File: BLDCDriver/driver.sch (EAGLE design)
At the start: 60 parts, among them Q2 SIZ240DT-T1-GE3, Q3 SIZ240DT-T1-GE3, Q4 SIZ240DT-T1-GE3, U1 QFN50P400X400X100-25NDRV8300D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, U2 AS5048A-HTSP-500, U4 SOP80P620X125-8N, X2 JST-XH-06-PIN-LONG-PAD

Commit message: 配線頑張った
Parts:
- removed D7, D8: WHITE, SparkFun-LED:LED-WHITE0603
- removed R21, R22: 1k, Custom_Designed_By_Yusei:RESISTOR-0603-1/10W-1%
- added C10, C18: 0.1UF, Custom_Designed_By_Yusei:0.1UF_1608
- added REG: AP7333, SOT95P237X112-3N:AP7333
- added U3: MCP2562-E/SN, MCP2562-E_SN:MCP2562-E/SN
- C13: value 0.1UF_1608 -> 0.1UF
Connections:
- net POWERLED_RESISTOR renamed L
- removed net LED1: D7.A
- removed net LED2: D8.A
- removed net N$12: D8.C, R21.1
- removed net N$13: D7.C, R22.1
- new net CANRX: U3.RXD
- new net CANTX: U3.TXD
- net 3V3: now also C10.1, REG.OUT, U3.VIO
- net 5V: now also C18.1, REG.IN, U3.VDD
- net CANH: now also U3.CANH
- net CANL: now also U3.CANL
- net GND: now also C10.2, C18.2, REG.GND, U3.STBY, U3.VSS; no longer R21.2, R22.2

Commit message: FETにビア通した
# ==== Emojis ====
# ✨ :sparkles: Add new feature
# ✅  :white_check_mark: Update existing feature (not bug)
# ⚠️  :warning: Fix bug/error
# 🔥  :fire: Remove files or features
# ✏️ :pencil2: Fix typos
# 📝  :memo: Update documentation
# ♻️  :recycle: Dependencies update
# 🐧  :penguin: Improved the Linux
# 🍎  :apple: Improved the macOS
# 🔖 :bookmark: Add new library
# 🎉  :tada: Initial commit

# ==== Format ====
# :emoji: Subject
#
# Commit body...

# ==== Messages ====
# 新規(ファイル)機能追加: Add
# 機能修正、既存機能追加（バグではない): Update
# リファクタリング: Clean
# ファイル名変更:
# 削除など: Remove
# バグ修正: Fix
# バージョンアップ: Upgrade
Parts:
- removed C13: 0.1UF, Custom_Designed_By_Yusei:0.1UF_1608
- added R21: 10k, Custom_Designed_By_Yusei:RESISTOR-0603-1/10W-1%
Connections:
- net 3V3: now also R21.1
- net GND: no longer C13.2
- net NRST: now also R21.2; no longer C13.1
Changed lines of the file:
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@@
 <setting verticaltext="up"/>
 </settings>
-<grid distance="0.05" unitdist="inch" unit="inch" style="lines" multiple="1" display="no" altdistance="0.01" altunitdist="inch" altunit="inch"/>
+<grid distance="0.1" unitdist="inch" unit="inch" style="lines" multiple="1" display="no" altdistance="0.01" altunitdist="inch" altunit="inch"/>
 <layers>
 <layer number="1" name="Top" color="4" fill="1" visible="no" active="no"/>
@@
 <part name="C11" library="SparkFun-Capacitors" deviceset="0.1UF" device="-0603-100V-10%" value="0.1uF"/>
 <part name="C12" library="SparkFun-Capacitors" deviceset="0.1UF" device="-0603-100V-10%" value="0.1uF"/>
-<part name="C13" library="Custom_Designed_By_Yusei" library_urn="urn:adsk.eagle:library:17377793" deviceset="0.1UF_1608" device="" package3d_urn="urn:adsk.eagle:package:17412407/2" value="0.1UF"/>
 <part name="GND17" library="supply" deviceset="GND" device=""/>
 <part name="R18" library="Custom_Designed_By_Yusei" library_urn="urn:adsk.eagle:library:17377793" deviceset="RESISTOR" device="-0603-1/10W-1%" package3d_urn="urn:adsk.eagle:package:17422883/2" value="10k"/>
@@
 <part name="C18" library="Custom_Designed_By_Yusei" library_urn="urn:adsk.eagle:library:17377793" deviceset="0.1UF_1608" device="" package3d_urn="urn:adsk.eagle:package:17412407/2" value="0.1UF"/>
 <part name="C10" library="Custom_Designed_By_Yusei" library_urn="urn:adsk.eagle:library:17377793" deviceset="0.1UF_1608" device="" package3d_urn="urn:adsk.eagle:package:17412407/2" value="0.1UF"/>
+<part name="R21" library="Custom_Designed_By_Yusei" library_urn="urn:adsk.eagle:library:17377793" deviceset="RESISTOR" device="-0603-1/10W-1%" package3d_urn="urn:adsk.eagle:package:17422883/2" value="10k"/>
 </parts>
 <sheets>
@@
 <attribute name="VALUE" x="169.164" y="197.231" size="1.778" layer="96" font="vector" rot="R270"/>
 </instance>
-<instance part="C13" gate="C$1" x="152.4" y="133.985" smashed="yes">
-<attribute name="NAME" x="153.924" y="136.906" size="1.778" layer="95" font="vector"/>
-</instance>
-<instance part="GND17" gate="1" x="152.4" y="126.365" smashed="yes">
-<attribute name="VALUE" x="149.86" y="123.825" size="1.778" layer="96"/>
+<instance part="GND17" gate="1" x="132.08" y="126.365" smashed="yes">
+<attribute name="VALUE" x="129.54" y="123.825" size="1.778" layer="96"/>
 </instance>
 <instance part="R18" gate="G$1" x="132.08" y="137.795" smashed="yes" rot="R90">
@@
 <instance part="C10" gate="C$1" x="229.87" y="57.15" smashed="yes">
 <attribute name="NAME" x="231.394" y="54.991" size="1.778" layer="95" font="vector"/>
+</instance>
+<instance part="R21" gate="G$1" x="157.48" y="137.16" smashed="yes" rot="R90">
+<attribute name="NAME" x="155.956" y="137.16" size="1.778" layer="95" font="vector" rot="R90" align="bottom-center"/>
+<attribute name="VALUE" x="159.004" y="137.16" size="1.778" layer="96" font="vector" rot="R90" align="top-center"/>
 </instance>
 </instances>
@@
 </segment>
 <segment>
-<pinref part="C13" gate="C$1" pin="2"/>
 <pinref part="GND17" gate="1" pin="GND"/>
-<wire x1="152.4" y1="131.445" x2="152.4" y2="128.905" width="0.1524" layer="91"/>
 <pinref part="R18" gate="G$1" pin="1"/>
 <wire x1="132.08" y1="132.715" x2="132.08" y2="128.905" width="0.1524" layer="91"/>
-<wire x1="132.08" y1="128.905" x2="152.4" y2="128.905" width="0.1524" layer="91"/>
-<junction x="152.4" y="128.905"/>
 <wire x1="119.38" y1="132.715" x2="119.38" y2="128.905" width="0.1524" layer="91"/>
 <wire x1="119.38" y1="128.905" x2="132.08" y2="128.905" width="0.1524" layer="91"/>
 <junction x="132.08" y="128.905"/>
-<label x="154.94" y="128.905" size="1.778" layer="95"/>
+<label x="121.92" y="126.365" size="1.778" layer="95"/>
 <pinref part="D3" gate="G$1" pin="C"/>
 </segment>
@@
 <junction x="229.87" y="62.23"/>
 </segment>
+<segment>
+<pinref part="R21" gate="G$1" pin="1"/>
+<wire x1="157.48" y1="132.08" x2="157.48" y2="129.54" width="0.1524" layer="91"/>
+<label x="157.48" y="129.54" size="0.762" layer="95" xref="yes"/>
+</segment>
 </net>
 <net name="C_V" class="0">
@@
 <net name="NRST" class="0">
 <segment>
-<label x="147.32" y="139.065" size="1.778" layer="95" rot="R180" xref="yes"/>
-<pinref part="C13" gate="C$1" pin="1"/>
-<wire x1="152.4" y1="139.065" x2="147.32" y2="139.065" width="0.1524" layer="91"/>
-</segment>
-<segment>
 <wire x1="12.7" y1="174.625" x2="33.02" y2="174.625" width="0.1524" layer="91"/>
 <label x="12.7" y="174.625" size="0.762" layer="95" rot="R180" xref="yes"/>
@@
 <label x="10.16" y="134.62" size="0.762" layer="95" rot="R180" xref="yes"/>
 </segment>
-</net>
+<segment>
+<pinref part="R21" gate="G$1" pin="2"/>
+<wire x1="157.48" y1="144.78" x2="157.48" y2="142.24" width="0.1524" layer="91"/>
+<label x="157.48" y="144.78" size="0.762" layer="95" xref="yes"/>
+</segment>
+</net>

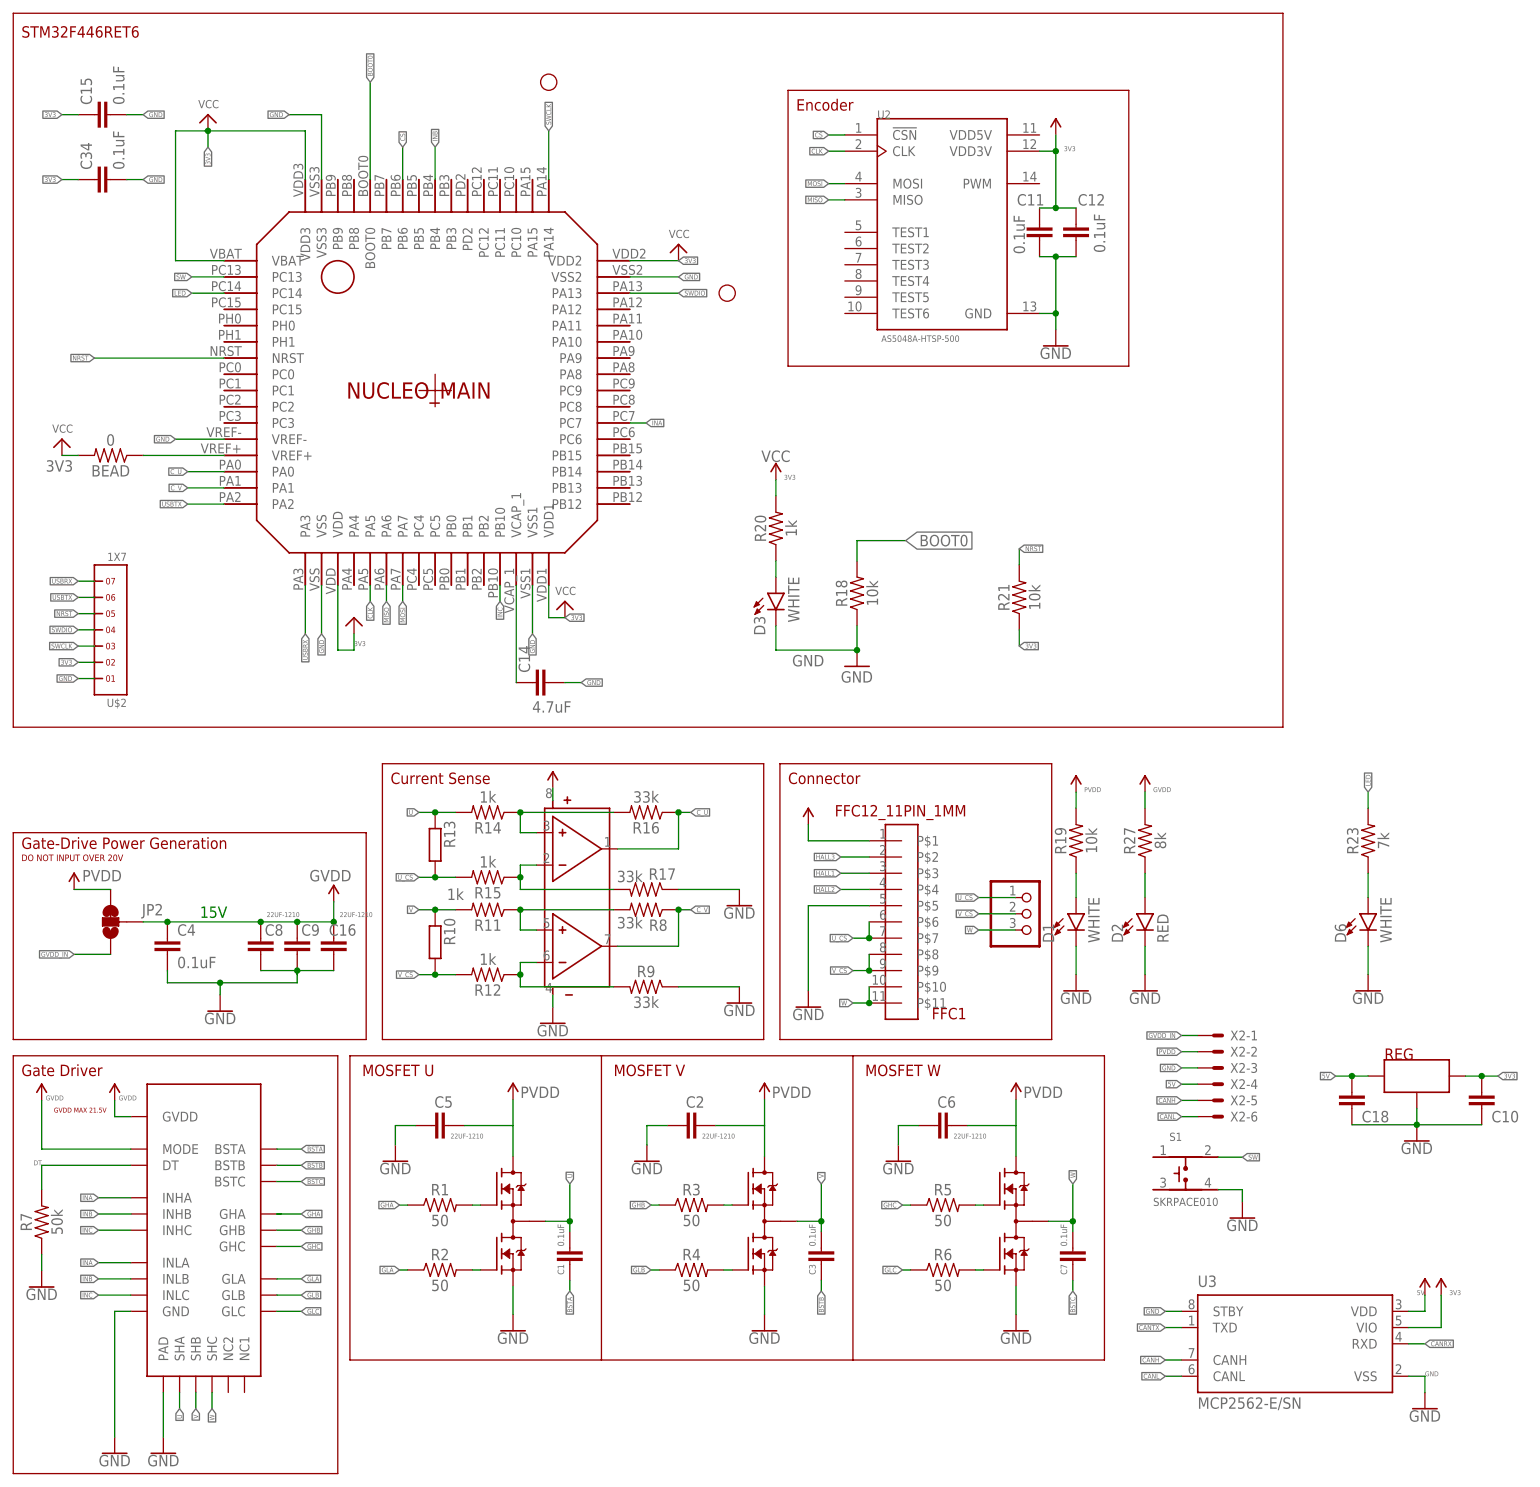
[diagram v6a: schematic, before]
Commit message: 配置プロった
- コンデンサを追加した。
- 電流センシングの相をVからWに変えた
- パワーラインから配線はじめた
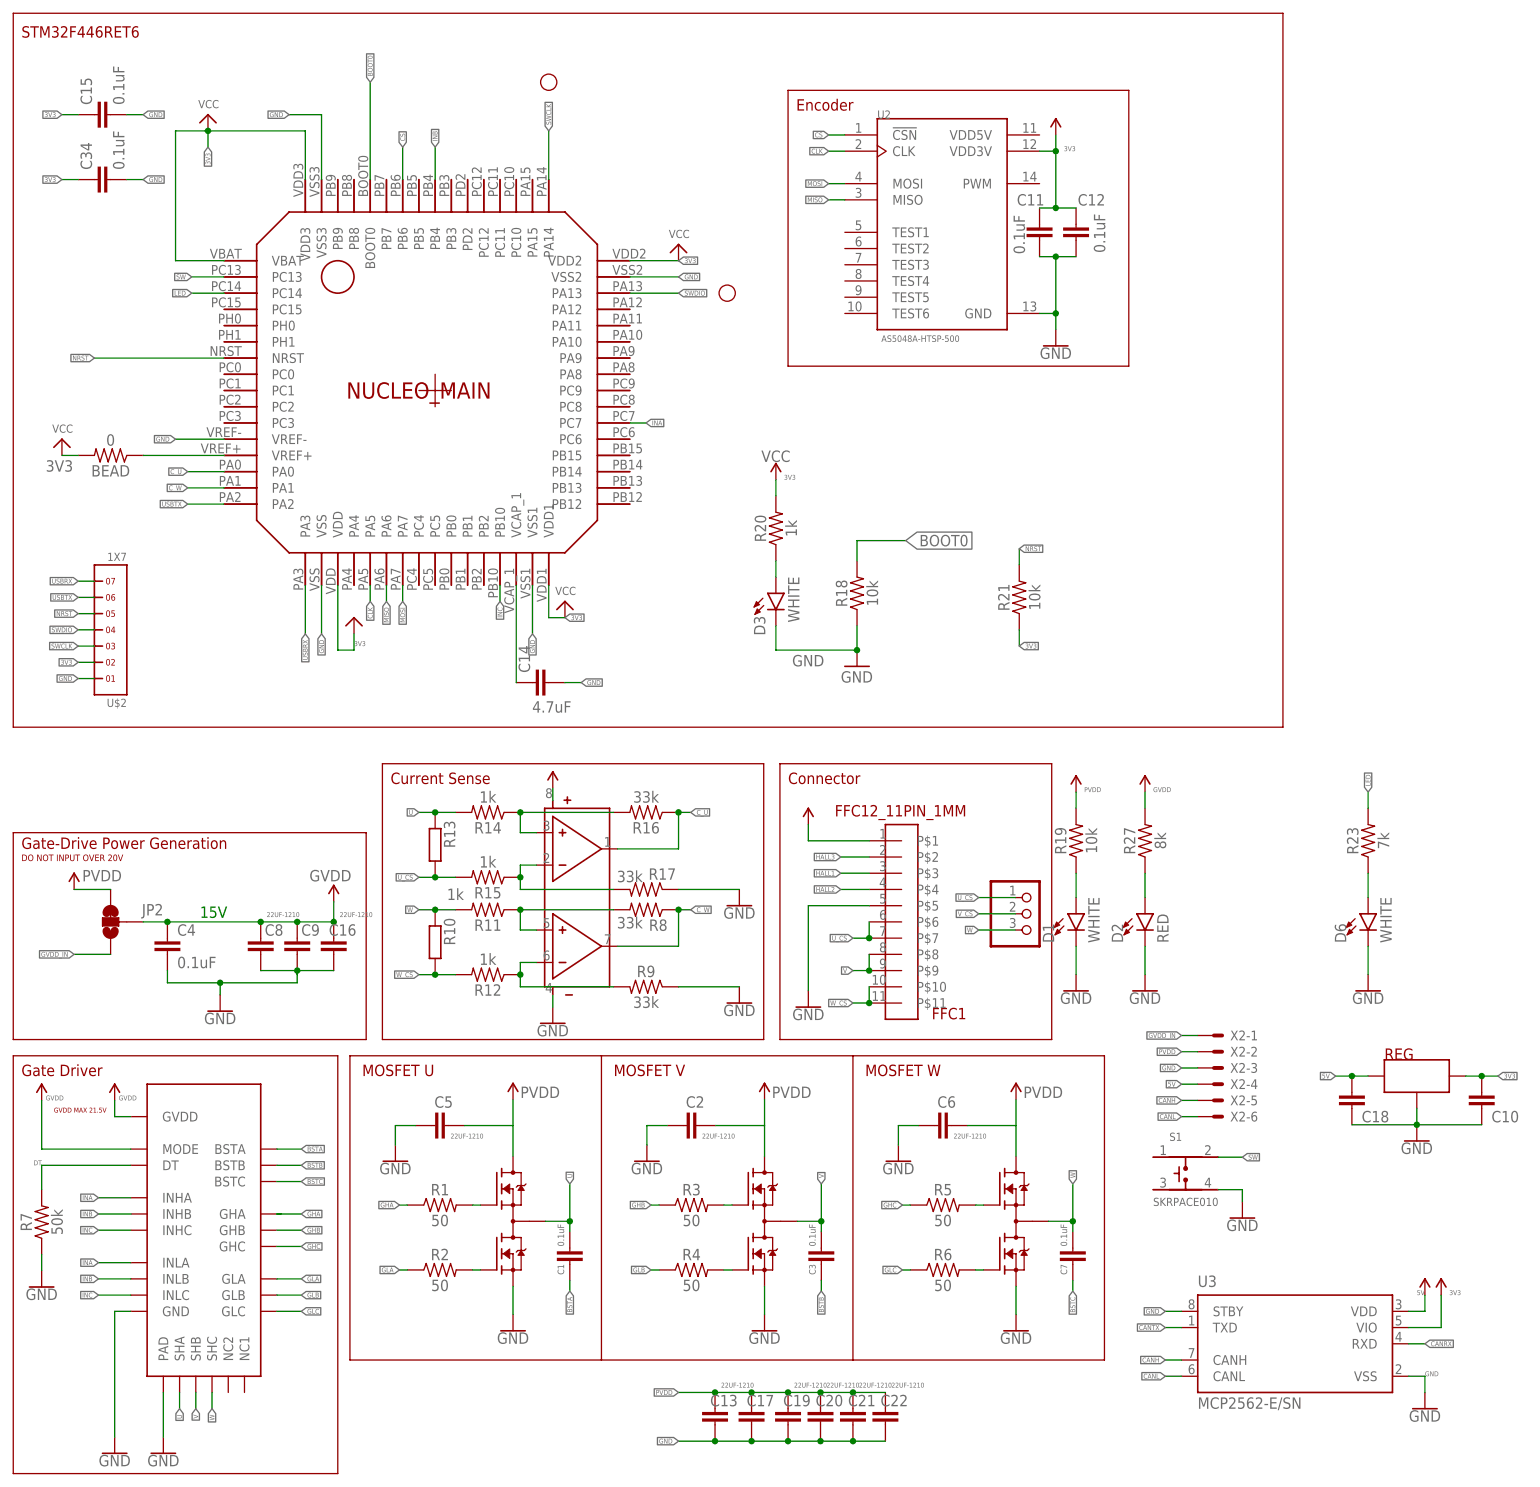
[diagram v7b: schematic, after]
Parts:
- added C13, C17, C19, C20, C21, C22: 22UF-1210, SparkFun-Capacitors:22UF-1210-16V-20%
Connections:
- net C_V renamed C_W
- new net W_CS: FFC1.P$10, FFC1.P$11, R10.1, R12.2
- net GND: now also C13.1, C17.1, C19.1, C20.1, C21.1, C22.1
- net PVDD: now also C13.2, C17.2, C19.2, C20.2, C21.2, C22.2
- net V: now also FFC1.P$8, FFC1.P$9; no longer R10.2, R11.2
- net V_CS: no longer FFC1.P$8, FFC1.P$9, R10.1, R12.2
- net W: now also R10.2, R11.2; no longer FFC1.P$10, FFC1.P$11

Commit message: いい感じ🦀
# ==== Emojis ====
# ✨ :sparkles: Add new feature
# ✅  :white_check_mark: Update existing feature (not bug)
# ⚠️  :warning: Fix bug/error
# 🔥  :fire: Remove files or features
# ✏️ :pencil2: Fix typos
# 📝  :memo: Update documentation
# ♻️  :recycle: Dependencies update
# 🐧  :penguin: Improved the Linux
# 🍎  :apple: Improved the macOS
# 🔖 :bookmark: Add new library
# 🎉  :tada: Initial commit

# ==== Format ====
# :emoji: Subject
#
# Commit body...

# ==== Messages ====
# 新規(ファイル)機能追加: Add
# 機能修正、既存機能追加（バグではない): Update
# リファクタリング: Clean
# ファイル名変更:
# 削除など: Remove
# バグ修正: Fix
# バージョンアップ: Upgrade
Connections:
- removed net V_CS: JP3.2
- net V: now also JP3.2
- net W: no longer JP3.3
- net W_CS: now also JP3.3
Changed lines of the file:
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@@
 <label x="131.445" y="78.74" size="0.762" layer="95" rot="MR0" xref="yes"/>
+</segment>
+<segment>
+<pinref part="JP3" gate="A" pin="2"/>
+<wire x1="156.845" y1="87.63" x2="151.13" y2="87.63" width="0.1524" layer="91"/>
+<label x="151.13" y="87.63" size="0.762" layer="95" rot="R180" xref="yes"/>
 </segment>
 </net>
@@
 </segment>
 <segment>
-<pinref part="JP3" gate="A" pin="3"/>
-<wire x1="156.845" y1="85.09" x2="151.13" y2="85.09" width="0.1524" layer="91"/>
-<label x="151.13" y="85.09" size="0.762" layer="95" rot="R180" xref="yes"/>
-</segment>
-<segment>
 <pinref part="R11" gate="G$1" pin="2"/>
 <wire x1="69.215" y1="88.265" x2="66.04" y2="88.265" width="0.1524" layer="91"/>
@@
 <wire x1="156.845" y1="90.17" x2="151.13" y2="90.17" width="0.1524" layer="91"/>
 <label x="151.13" y="90.17" size="0.762" layer="95" rot="R180" xref="yes"/>
-</segment>
-</net>
-<net name="V_CS" class="0">
-<segment>
-<pinref part="JP3" gate="A" pin="2"/>
-<wire x1="156.845" y1="87.63" x2="151.13" y2="87.63" width="0.1524" layer="91"/>
-<label x="151.13" y="87.63" size="0.762" layer="95" rot="R180" xref="yes"/>
 </segment>
 </net>
@@
 <label x="131.445" y="73.66" size="0.762" layer="95" rot="MR0" xref="yes"/>
 </segment>
-</net>
+<segment>
+<pinref part="JP3" gate="A" pin="3"/>
+<wire x1="156.845" y1="85.09" x2="151.13" y2="85.09" width="0.1524" layer="91"/>
+<label x="151.13" y="85.09" size="0.762" layer="95" rot="R180" xref="yes"/>
+</segment>
+</net>
